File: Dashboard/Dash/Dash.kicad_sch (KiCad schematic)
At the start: 32 parts, among them IC1 MCP25625-E_SS, J1 TACH-SERVO, J2 SPEED-SERVO, J4 UPPER Button, J6 LOWER Button, J7 DTF13-6P, U1 XIAO-ESP32-S3-SMD, U3 EA DOGM128W-6, Y1 ABM10AIG-16.000MHZ-4Z-T3

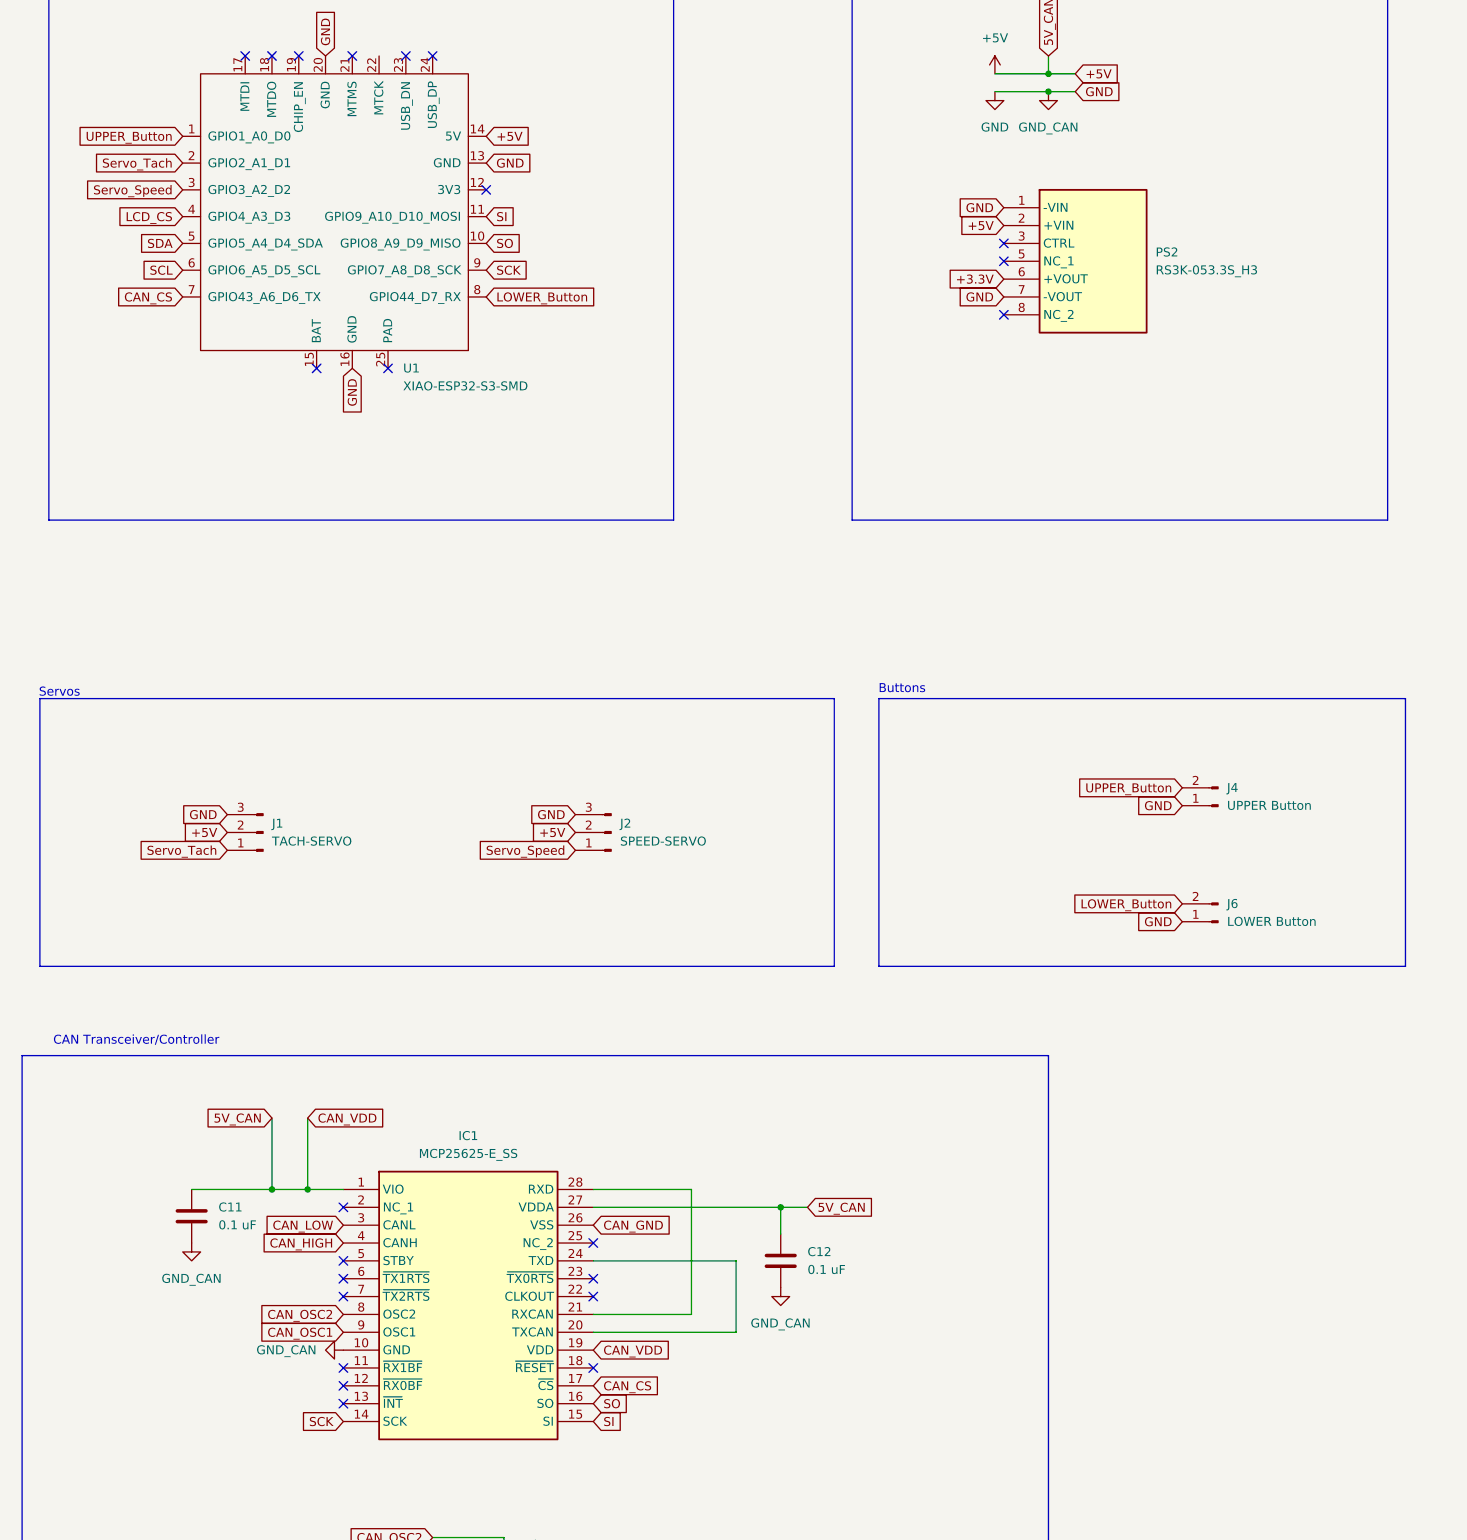
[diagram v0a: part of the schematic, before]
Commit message: Swapped upper button for CAN_INT
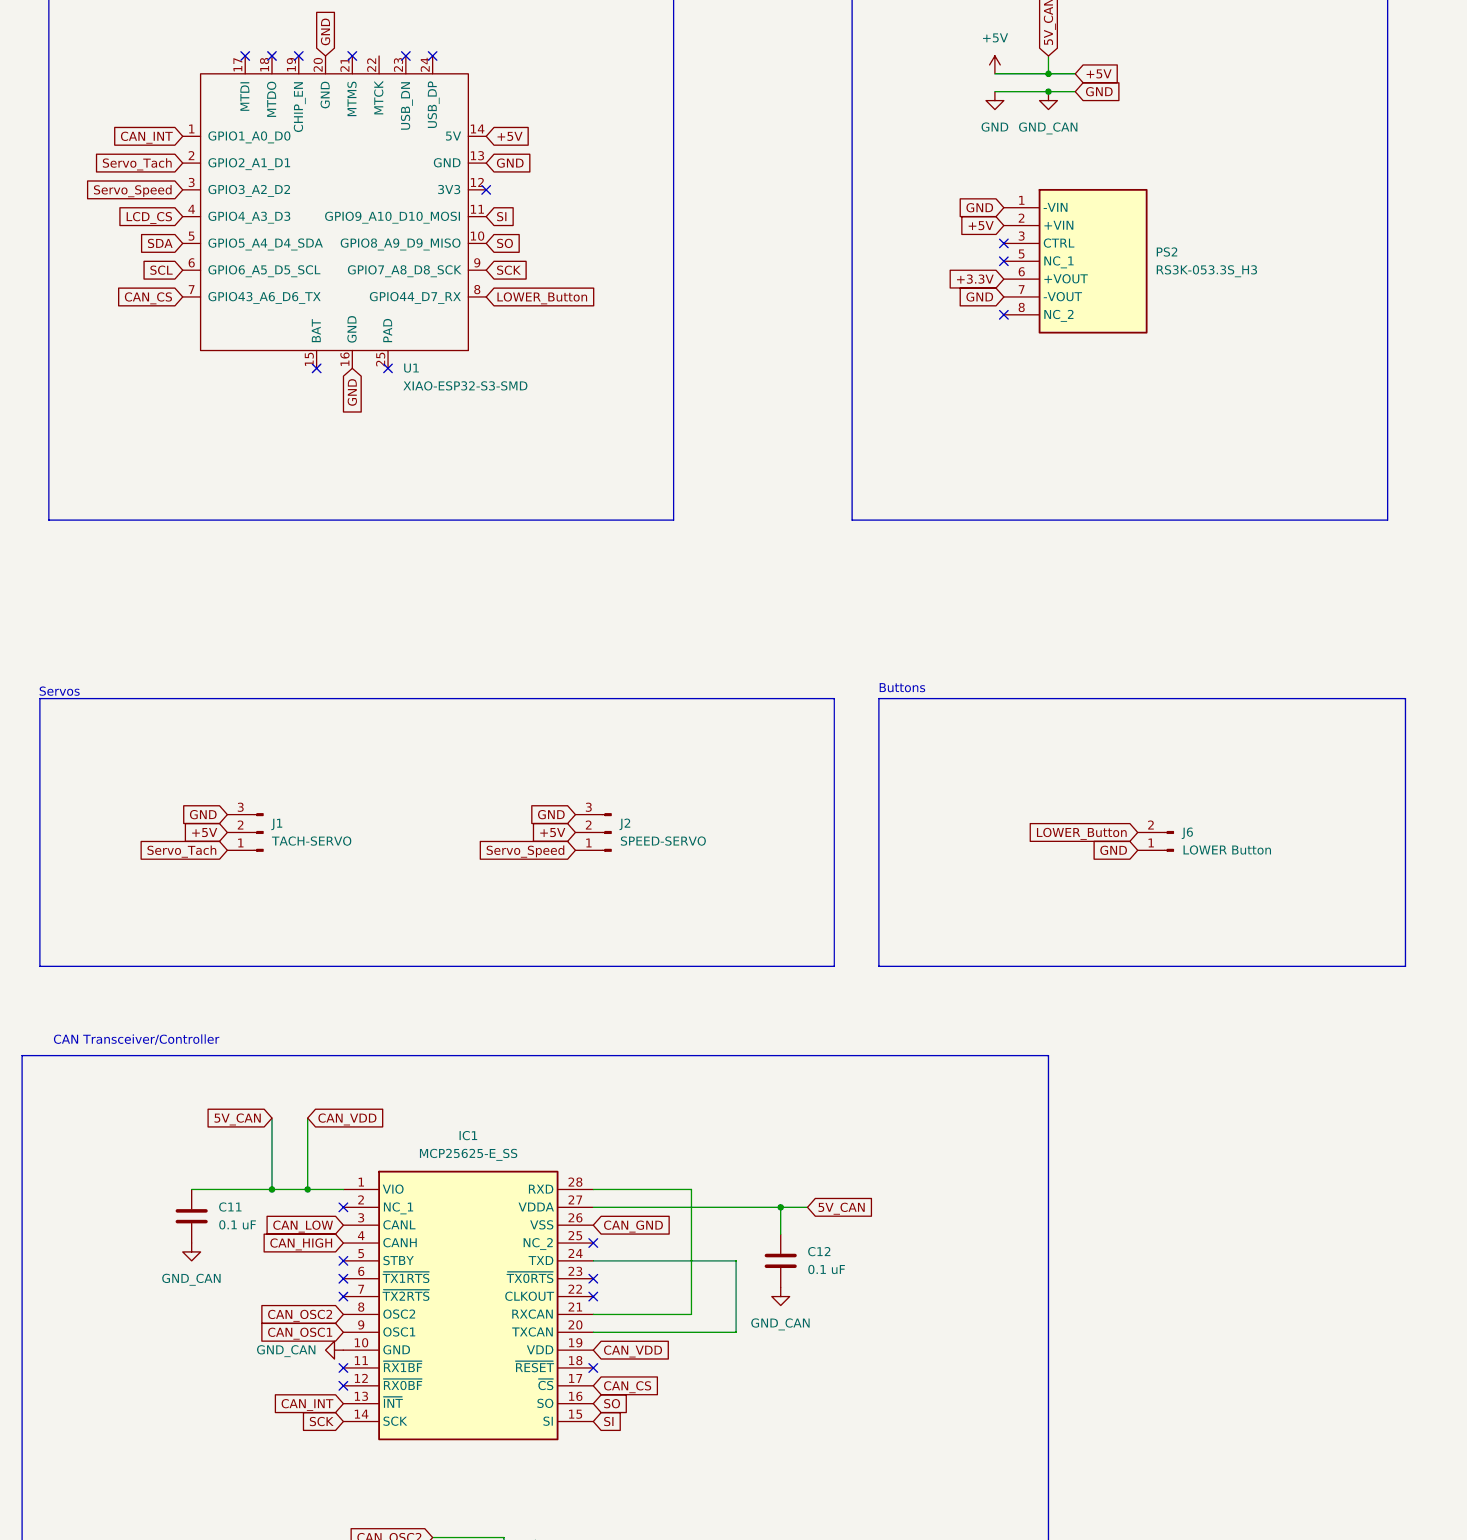
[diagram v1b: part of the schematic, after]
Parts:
- removed J4: UPPER Button, Connector_PinHeader_2.54mm:PinHeader_1x02_P2.54mm_Vertical, symbol Connector:Conn_01x02_Pin
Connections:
- net UPPER_Button is gone; now on net CAN_INT: U1.1 (GPIO1_A0_D0)
- net CAN_INT: now reaches IC1.13 (~{INT})
- no-connect marks 37 -> 36
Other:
- moved on the sheet: J6
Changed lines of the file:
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@@
 	)
 	(no_connect
-		(at 67.31 227.33)
-	)
-	(no_connect
 		(at 63.5 80.01)
 	)
@@
 	(global_label "GND"
 		(shape input)
-		(at 186.69 158.75 180)
+		(at 180.34 148.59 180)
 		(fields_autoplaced yes)
 		(effects
@@
 		)
 		(property "Intersheetrefs" "${INTERSHEET_REFS}"
-			(at 179.8343 158.75 0)
+			(at 173.4843 148.59 0)
 			(effects
 				(font
@@
 		)
 	)
-	(global_label "UPPER_Button"
-		(shape input)
-		(at 186.69 139.7 180)
-		(fields_autoplaced yes)
-		(effects
-			(font
-				(size 1.27 1.27)
-			)
-			(justify right)
-		)
-		(property "Intersheetrefs" "${INTERSHEET_REFS}"
-			(at 170.2793 139.7 0)
-			(effects
-				(font
-					(size 1.27 1.27)
-				)
-				(justify right)
-				(hide yes)
-			)
-		)
-	)
 	(global_label "ROW11_UPPER"
 		(shape input)
@@
 	(global_label "LOWER_Button"
 		(shape input)
-		(at 186.69 156.21 180)
+		(at 180.34 146.05 180)
 		(fields_autoplaced yes)
 		(effects
@@
 		)
 		(property "Intersheetrefs" "${INTERSHEET_REFS}"
-			(at 170.3398 156.21 0)
+			(at 163.9898 146.05 0)
 			(effects
 				(font
@@
 	(global_label "GND"
 		(shape input)
-		(at 186.69 142.24 180)
-		(fields_autoplaced yes)
-		(effects
-			(font
-				(size 1.27 1.27)
-			)
-			(justify right)
-		)
-		(property "Intersheetrefs" "${INTERSHEET_REFS}"
-			(at 179.8343 142.24 0)
-			(effects
-				(font
-					(size 1.27 1.27)
-				)
-				(justify right)
-				(hide yes)
-			)
-		)
-	)
-	(global_label "GND"
-		(shape input)
 		(at 266.7 182.88 180)
 		(fields_autoplaced yes)
@@
 		)
 	)
+	(global_label "CAN_INT"
+		(shape input)
+		(at 44.45 46.99 180)
+		(fields_autoplaced yes)
+		(effects
+			(font
+				(size 1.27 1.27)
+			)
+			(justify right)
+		)
+		(property "Intersheetrefs" "${INTERSHEET_REFS}"
+			(at 33.9052 46.99 0)
+			(effects
+				(font
+					(size 1.27 1.27)
+				)
+				(justify right)
+				(hide yes)
+			)
+		)
+	)
 	(global_label "ROW10_UPPER"
 		(shape input)
@@
 		)
 	)
+	(global_label "CAN_INT"
+		(shape input)
+		(at 67.31 227.33 180)
+		(fields_autoplaced yes)
+		(effects
+			(font
+				(size 1.27 1.27)
+			)
+			(justify right)
+		)
+		(property "Intersheetrefs" "${INTERSHEET_REFS}"
+			(at 56.7652 227.33 0)
+			(effects
+				(font
+					(size 1.27 1.27)
+				)
+				(justify right)
+				(hide yes)
+			)
+		)
+	)
 	(global_label "COM_Digit2_UPPER"
 		(shape input)
@@
 		)
 	)
-	(global_label "UPPER_Button"
-		(shape input)
-		(at 44.45 46.99 180)
-		(fields_autoplaced yes)
-		(effects
-			(font
-				(size 1.27 1.27)
-			)
-			(justify right)
-		)
-		(property "Intersheetrefs" "${INTERSHEET_REFS}"
-			(at 28.0393 46.99 0)
-			(effects
-				(font
-					(size 1.27 1.27)
-				)
-				(justify right)
-				(hide yes)
-			)
-		)
-	)
 	(global_label "GND"
 		(shape input)
@@
 	)
 	(symbol
-		(lib_id "Connector:Conn_01x02_Pin")
-		(at 191.77 142.24 180)
-		(unit 1)
-		(exclude_from_sim no)
-		(in_bom yes)
-		(on_board yes)
-		(dnp no)
-		(fields_autoplaced yes)
-		(property "Reference" "J4"
-			(at 193.04 139.6999 0)
-			(effects
-				(font
-					(size 1.27 1.27)
-				)
-				(justify right)
-			)
-		)
-		(property "Value" "UPPER Button"
-			(at 193.04 142.2399 0)
-			(effects
-				(font
-					(size 1.27 1.27)
-				)
-				(justify right)
-			)
-		)
-		(property "Footprint" "Connector_PinHeader_2.54mm:PinHeader_1x02_P2.54mm_Vertical"
-			(at 191.77 142.24 0)
-			(effects
-				(font
-					(size 1.27 1.27)
-				)
-				(hide yes)
-			)
-		)
-		(property "Datasheet" "~"
-			(at 191.77 142.24 0)
-			(effects
-				(font
-					(size 1.27 1.27)
-				)
-				(hide yes)
-			)
-		)
-		(property "Description" "Generic connector, single row, 01x02, script generated"
-			(at 191.77 142.24 0)
-			(effects
-				(font
-					(size 1.27 1.27)
-				)
-				(hide yes)
-			)
-		)
-		(pin "1"
-		)
-		(pin "2"
-		)
-		(instances
-			(project ""
-				(path "/514ba468-47e0-43f8-9194-8a3a232891b9"
-					(reference "J4")
-					(unit 1)
-				)
-			)
-		)
-	)
-	(symbol
 		(lib_id "Device:C")
 		(at 45.72 200.66 0)
@@
 	(symbol
 		(lib_id "Connector:Conn_01x02_Pin")
-		(at 191.77 158.75 180)
+		(at 185.42 148.59 180)
 		(unit 1)
 		(exclude_from_sim no)
@@
 		(fields_autoplaced yes)
 		(property "Reference" "J6"
-			(at 193.04 156.2099 0)
+			(at 186.69 146.0499 0)
 			(effects
 				(font
@@
 		)
 		(property "Value" "LOWER Button"
-			(at 193.04 158.7499 0)
+			(at 186.69 148.5899 0)
 			(effects
 				(font
@@
 		)
 		(property "Footprint" "Connector_PinHeader_2.54mm:PinHeader_1x02_P2.54mm_Vertical"
-			(at 191.77 158.75 0)
+			(at 185.42 148.59 0)
 			(effects
 				(font
@@
 		)
 		(property "Datasheet" "~"
-			(at 191.77 158.75 0)
+			(at 185.42 148.59 0)
 			(effects
 				(font
@@
 		)
 		(property "Description" "Generic connector, single row, 01x02, script generated"
-			(at 191.77 158.75 0)
+			(at 185.42 148.59 0)
 			(effects
 				(font

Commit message: Fixed Schematic and Removed CAN_GND on CAN chip
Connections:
- net CAN_GND is gone; now on net GND: IC1.26 (VSS)
- net ROW14_LOWER: now also LOWER_D1-2.8 (A_DP), LOWER_D3-4.8 (A_DP)
- net ROW14_UPPER: no longer LOWER_D1-2.8 (A_DP), LOWER_D3-4.8 (A_DP)
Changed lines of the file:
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@@
 		)
 	)
-	(global_label "CAN_GND"
+	(global_label "GND"
 		(shape input)
 		(at 102.87 201.93 0)
@@
 		)
 		(property "Intersheetrefs" "${INTERSHEET_REFS}"
-			(at 114.3824 201.93 0)
+			(at 109.7257 201.93 0)
 			(effects
 				(font
@@
 		)
 	)
-	(global_label "ROW14_UPPER"
+	(global_label "ROW14_LOWER"
 		(shape input)
 		(at 411.48 106.68 180)
@@
 		)
 		(property "Intersheetrefs" "${INTERSHEET_REFS}"
-			(at 394.7668 106.68 0)
+			(at 394.8273 106.68 0)
 			(effects
 				(font
@@
 		)
 	)
-	(global_label "ROW14_UPPER"
+	(global_label "ROW14_LOWER"
 		(shape input)
 		(at 501.65 106.68 180)
@@
 		)
 		(property "Intersheetrefs" "${INTERSHEET_REFS}"
-			(at 484.9368 106.68 0)
+			(at 484.9973 106.68 0)
 			(effects
 				(font
